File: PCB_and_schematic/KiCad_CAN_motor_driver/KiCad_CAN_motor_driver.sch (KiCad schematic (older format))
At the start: 59 parts, among them J1 SWDIO, J2 UART, J3 POWER IN 24V, J4 MOTOR OUT, J5 CAN, J6 PWM IN, Q1 BTN8982TA, Q2 BTN8982TA, U1 SN65HVD232, U2 LMR50410, U3 STM32F103C8Tx

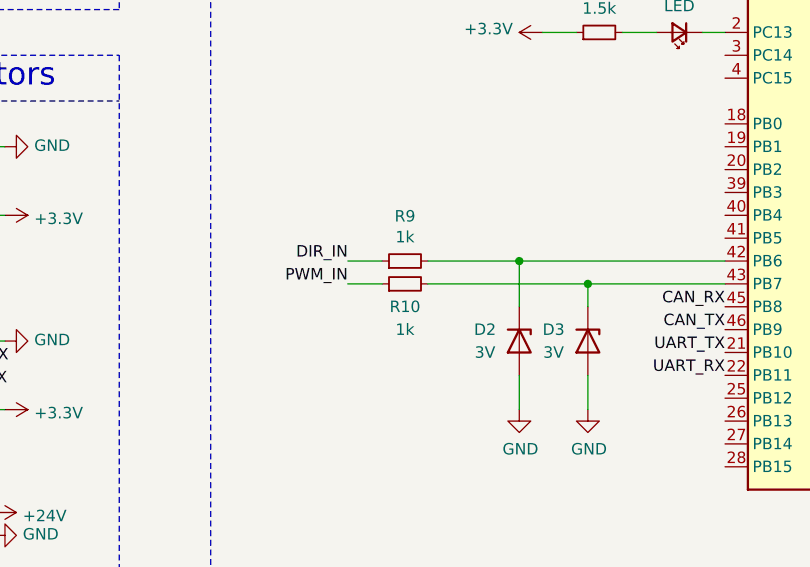
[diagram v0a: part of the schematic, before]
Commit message: PDF schematic
+ schematic in PDF format for quick preview
+ changed resistors on PWM inputs from 1K to 6.8K to decrease Zener diodes current
+ little tweaks in PCB traces
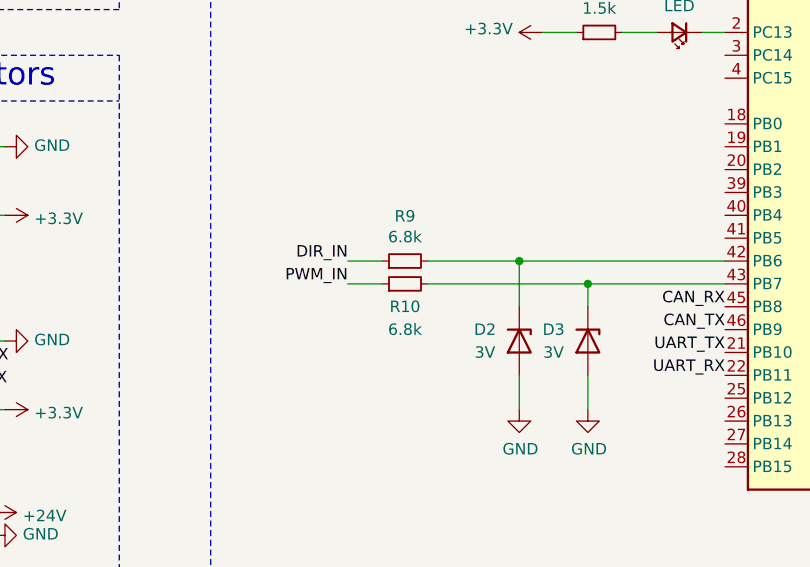
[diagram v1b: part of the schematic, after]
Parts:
- R10, R9: value 1k -> 6.8k
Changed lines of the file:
@@
 P 8650 4850
 F 0 "R9" V 8846 4850 50  0000 C CNN
-F 1 "1k" V 8755 4850 50  0000 C CNN
+F 1 "6.8k" V 8755 4850 50  0000 C CNN
 F 2 "Resistor_SMD:R_1206_3216Metric_Pad1.30x1.75mm_HandSolder" H 8650 4850 50  0001 C CNN
 F 3 "~" H 8650 4850 50  0001 C CNN
@@
 P 8650 4950
 F 0 "R10" V 8550 4950 50  0000 C CNN
-F 1 "1k" V 8450 4950 50  0000 C CNN
+F 1 "6.8k" V 8450 4950 50  0000 C CNN
 F 2 "Resistor_SMD:R_1206_3216Metric_Pad1.30x1.75mm_HandSolder" H 8650 4950 50  0001 C CNN
 F 3 "~" H 8650 4950 50  0001 C CNN

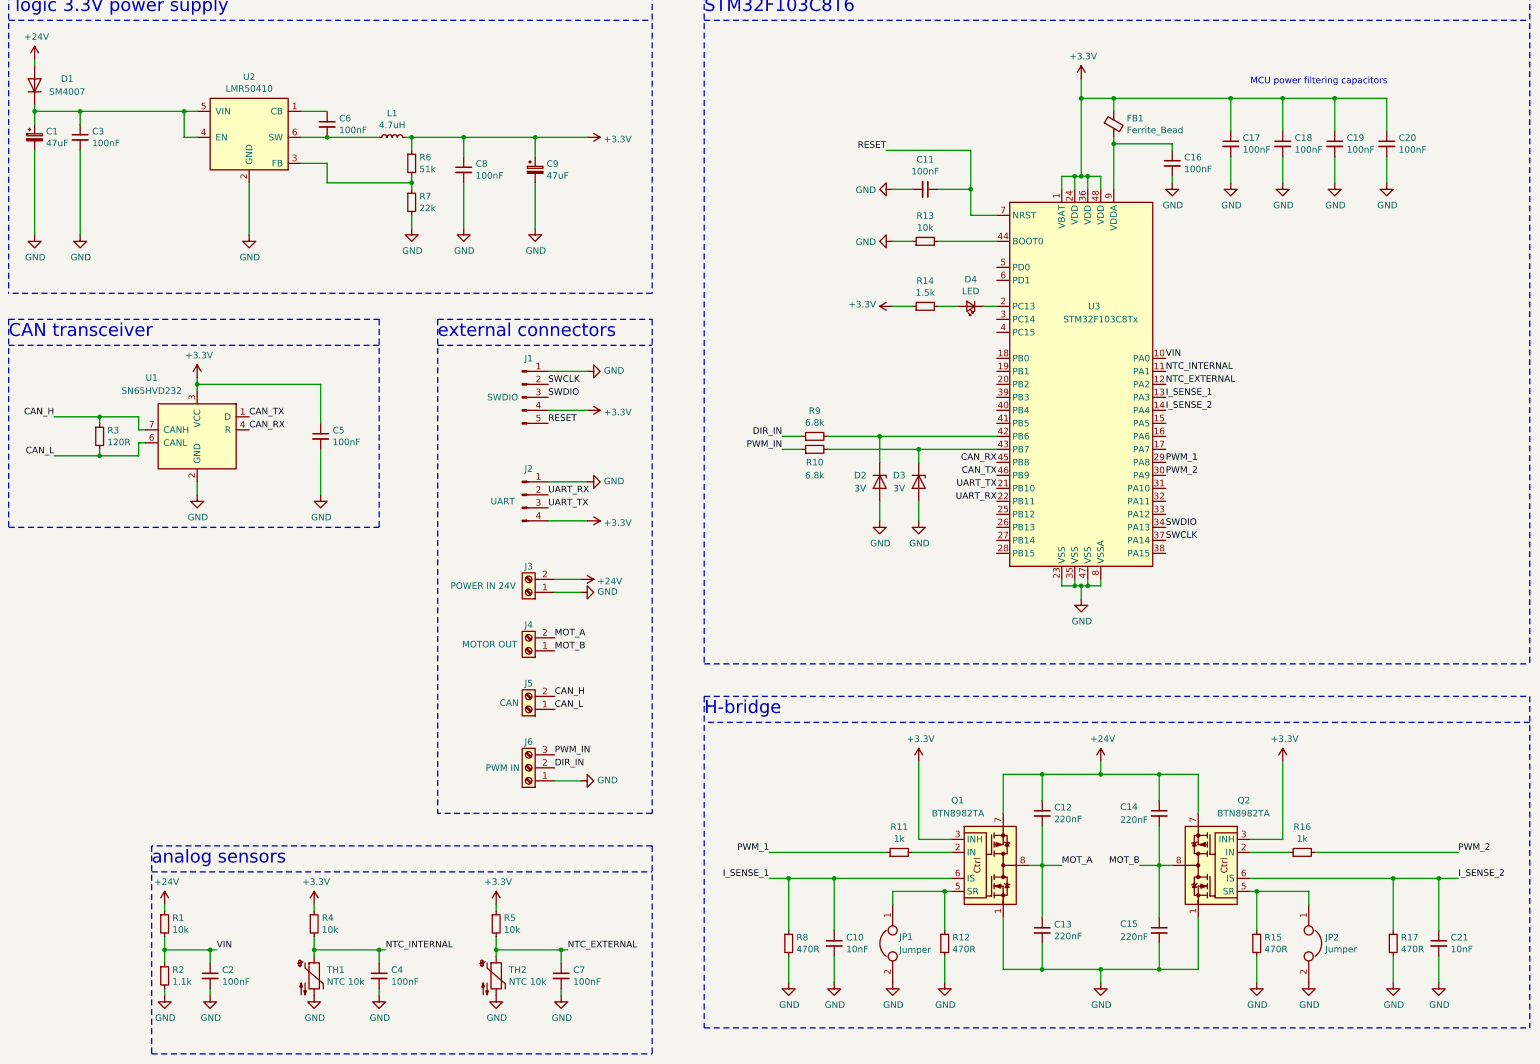
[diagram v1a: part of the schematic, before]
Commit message: Added vias on power traces near input, added testpoints
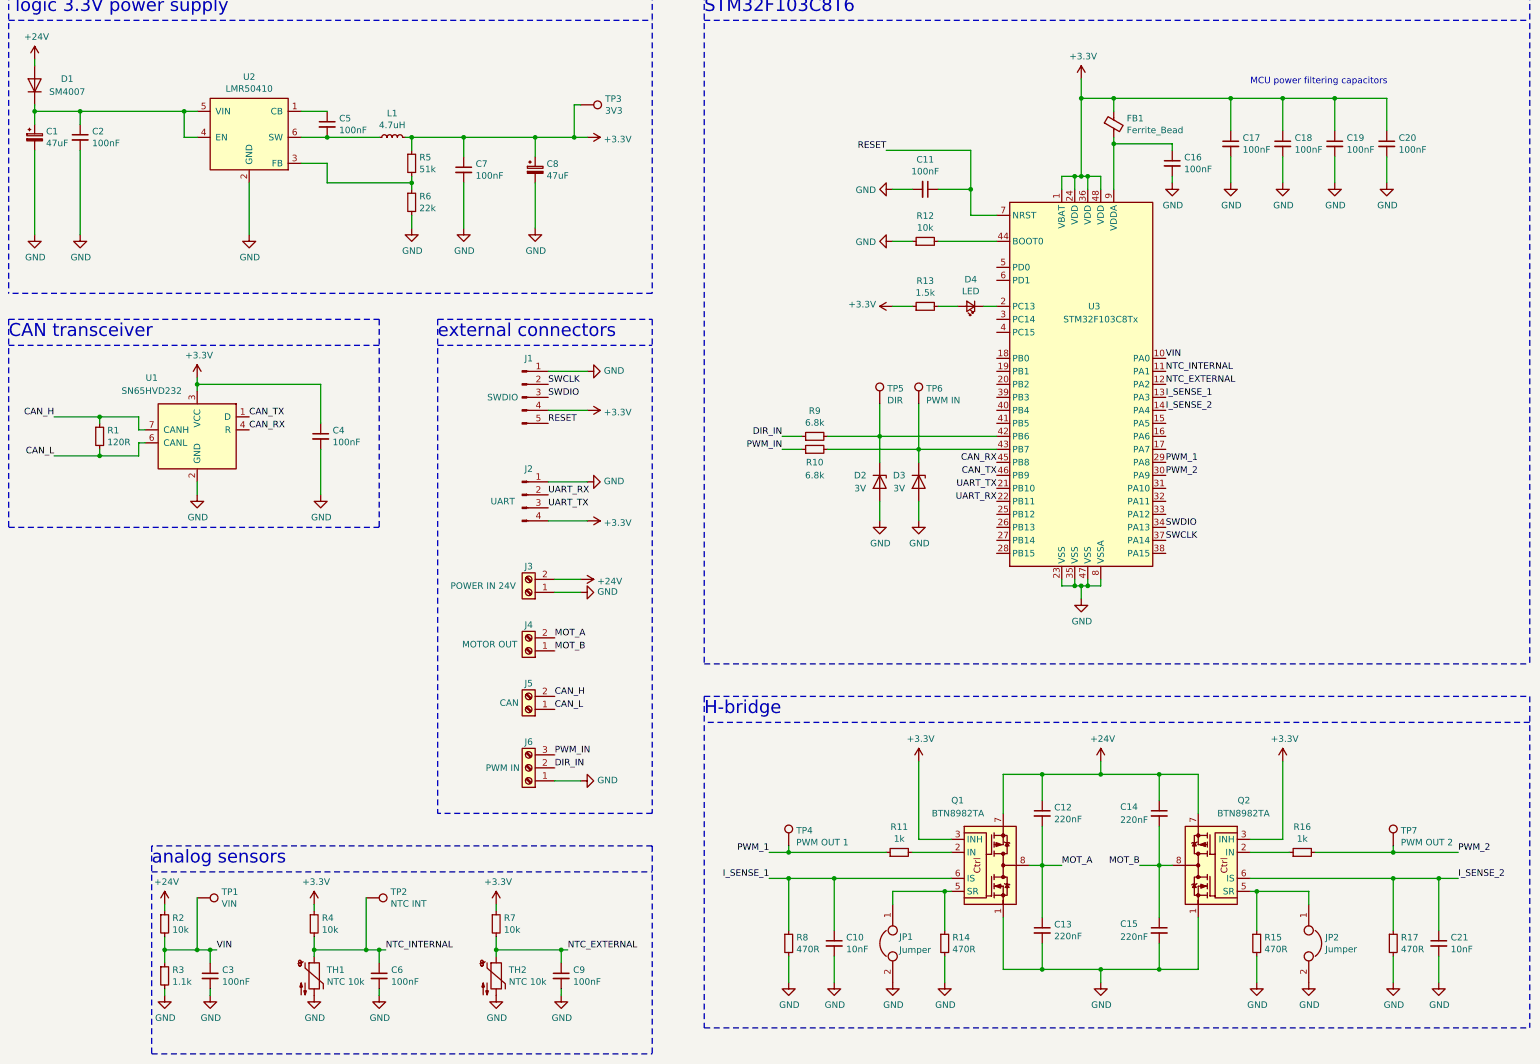
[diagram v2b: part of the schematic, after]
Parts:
- added TP1: VIN, TestPoint:TestPoint_THTPad_D1.0mm_Drill0.5mm, symbol Connector:TestPoint
- added TP2: NTC INT, TestPoint:TestPoint_THTPad_D1.0mm_Drill0.5mm, symbol Connector:TestPoint
- added TP3: 3V3, TestPoint:TestPoint_THTPad_D1.0mm_Drill0.5mm, symbol Connector:TestPoint
- added TP4: PWM OUT 1, TestPoint:TestPoint_THTPad_D1.0mm_Drill0.5mm, symbol Connector:TestPoint
- added TP5: DIR, TestPoint:TestPoint_THTPad_D1.0mm_Drill0.5mm, symbol Connector:TestPoint
- added TP6: PWM IN, TestPoint:TestPoint_THTPad_D1.0mm_Drill0.5mm, symbol Connector:TestPoint
- added TP7: PWM OUT 2, TestPoint:TestPoint_THTPad_D1.0mm_Drill0.5mm, symbol Connector:TestPoint
- renumbered C3 to C2, C2 to C3, C5 to C4, C6 to C5, C4 to C6, C8 to C7, C9 to C8, C7 to C9, R3 to R1, R13 to R12, R14 to R13, R12 to R14, R1 to R2, R2 to R3, R6 to R5, R7 to R6, R5 to R7
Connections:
- net +3V3: now also TP3.1
- net NTC_INTERNAL: now also TP2.1
- net PWM_1: now also TP4.1
- net PWM_2: now also TP7.1
- net VIN: now also TP1.1
- net at D2.1 (K), R9.2, U3.42 (PB6): now also TP5.1
- net at D3.1 (K), R10.2, U3.43 (PB7): now also TP6.1

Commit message: Final PCB version (rev 1.0)
+ reduced amount of vias
+ increased distance between vias
+ removed vias from half-bridge's bottom and moved them closer to motor output pads
+ changed PWM input connector to goldpin
+ added jumper (default open) connecting terminating resistor to CAN bus

+ updated PDF schematic
+updated 3D models
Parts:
- removed J6: PWM IN, WK_lib:PowerPad_3x_3mm, symbol Connector:Screw_Terminal_01x03
- added J6: PWM_IN, Connector_PinHeader_2.54mm:PinHeader_1x03_P2.54mm_Vertical, symbol Connector:Conn_01x03_Male
- added JP3: Jumper, Jumper:SolderJumper-2_P1.3mm_Open_Pad1.0x1.5mm, symbol Device:Jumper
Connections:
- net CAN_L: now also JP3.2; no longer R1.2
- net DIR_IN: now also J6.2 (Pin_2)
- net GND: now also J6.3 (Pin_3)
- net PWM_IN: now also J6.1 (Pin_1)
- new net: JP3.1, R1.2
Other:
- moved on the sheet: R1
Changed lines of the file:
@@
 Text Label 6650 6850 0    50   ~ 0
 CAN_H
-$Comp
-L Connector:Screw_Terminal_01x03 J6
-U 1 1 6063F28F
-P 6450 7400
-F 0 "J6" H 6450 7200 50  0000 C CNN
-F 1 "PWM IN" H 6650 7400 50  0000 C CNN
-F 2 "WK_lib:PowerPad_3x_3mm" H 6450 7400 50  0001 C CNN
-F 3 "~" H 6450 7400 50  0001 C CNN
-	1    6450 7400
-	-1   0    0    1
-$EndComp
 Text Label 6650 7300 0    50   ~ 0
 PWM_IN
@@
 $EndComp
 Wire Wire Line
-	6650 7500 6850 7500
+	6600 7500 6850 7500
 Wire Notes Line
 	7400 7750 5750 7750
@@
 Wire Notes Line
 	5750 3950 5750 7750
-$Comp
-L Interface_CAN_LIN:SN65HVD232 U1
-U 1 1 60673CE3
-P 3900 4800
-F 0 "U1" H 4250 5200 50  0000 C CNN
-F 1 "SN65HVD232" H 4250 5100 50  0000 C CNN
-F 2 "Package_SO:SOIC-8_3.9x4.9mm_P1.27mm" H 3900 4300 50  0001 C CNN
-F 3 "http://www.ti.com/lit/ds/symlink/sn65hvd230.pdf" H 3800 5200 50  0001 C CNN
-	1    3900 4800
-	-1   0    0    -1
-$EndComp
-$Comp
-L power:+3.3V #PWR06
-U 1 1 60676560
-P 3900 4400
-F 0 "#PWR06" H 3900 4250 50  0001 C CNN
-F 1 "+3.3V" H 3915 4573 50  0000 C CNN
-F 2 "" H 3900 4400 50  0001 C CNN
-F 3 "" H 3900 4400 50  0001 C CNN
-	1    3900 4400
-	1    0    0    -1
-$EndComp
-$Comp
-L power:GND #PWR07
-U 1 1 606775A4
-P 3900 5300
-F 0 "#PWR07" H 3900 5050 50  0001 C CNN
-F 1 "GND" H 3905 5127 50  0000 C CNN
-F 2 "" H 3900 5300 50  0001 C CNN
-F 3 "" H 3900 5300 50  0001 C CNN
-	1    3900 5300
-	1    0    0    -1
-$EndComp
-Text Label 4300 4700 0    50   ~ 0
-CAN_TX
-Text Label 4300 4800 0    50   ~ 0
-CAN_RX
-Wire Wire Line
-	3900 4400 3900 4450
-Wire Wire Line
-	3900 5200 3900 5300
-Text Label 2800 4700 2    50   ~ 0
-CAN_H
-Text Label 2800 5000 2    50   ~ 0
-CAN_L
-$Comp
-L Device:R_Small R1
-U 1 1 60686C82
-P 3150 4850
-F 0 "R1" H 3209 4896 50  0000 L CNN
-F 1 "120R" H 3209 4805 50  0000 L CNN
-F 2 "Resistor_SMD:R_1206_3216Metric_Pad1.30x1.75mm_HandSolder" H 3150 4850 50  0001 C CNN
-F 3 "~" H 3150 4850 50  0001 C CNN
-	1    3150 4850
-	1    0    0    -1
-$EndComp
-Wire Wire Line
-	3500 4800 3450 4800
-Wire Wire Line
-	3450 4800 3450 4700
-Wire Wire Line
-	3450 4700 3150 4700
-Wire Wire Line
-	3500 4900 3450 4900
-Wire Wire Line
-	3450 4900 3450 5000
-Wire Wire Line
-	3450 5000 3150 5000
-Wire Wire Line
-	3150 4950 3150 5000
-Connection ~ 3150 5000
-Wire Wire Line
-	3150 5000 2800 5000
-Wire Wire Line
-	3150 4750 3150 4700
-Connection ~ 3150 4700
-Wire Wire Line
-	3150 4700 2800 4700
-$Comp
-L Device:C_Small C4
-U 1 1 606A1169
-P 4850 4850
-F 0 "C4" H 4942 4896 50  0000 L CNN
-F 1 "100nF" H 4942 4805 50  0000 L CNN
-F 2 "Capacitor_SMD:C_1206_3216Metric_Pad1.33x1.80mm_HandSolder" H 4850 4850 50  0001 C CNN
-F 3 "~" H 4850 4850 50  0001 C CNN
-	1    4850 4850
-	1    0    0    -1
-$EndComp
-Wire Wire Line
-	3900 4450 4850 4450
-Wire Wire Line
-	4850 4450 4850 4750
-Connection ~ 3900 4450
-Wire Wire Line
-	3900 4450 3900 4500
-Wire Wire Line
-	4850 4950 4850 5300
-$Comp
-L power:GND #PWR012
-U 1 1 606AA75D
-P 4850 5300
-F 0 "#PWR012" H 4850 5050 50  0001 C CNN
-F 1 "GND" H 4855 5127 50  0000 C CNN
-F 2 "" H 4850 5300 50  0001 C CNN
-F 3 "" H 4850 5300 50  0001 C CNN
-	1    4850 5300
-	1    0    0    -1
-$EndComp
 Wire Notes Line
 	5300 4150 2450 4150
@@
 Wire Wire Line
 	6200 8800 6700 8800
+$Comp
+L Connector:Conn_01x03_Male J6
+U 1 1 605AD111
+P 6400 7400
+F 0 "J6" H 6450 7600 50  0000 C CNN
+F 1 "PWM_IN" H 6250 7400 50  0000 C CNN
+F 2 "Connector_PinHeader_2.54mm:PinHeader_1x03_P2.54mm_Vertical" H 6400 7400 50  0001 C CNN
+F 3 "~" H 6400 7400 50  0001 C CNN
+	1    6400 7400
+	1    0    0    -1
+$EndComp
+Wire Wire Line
+	6650 7300 6600 7300
+Wire Wire Line
+	6650 7400 6600 7400
+$Comp
+L power:GND #PWR012
+U 1 1 606AA75D
+P 4850 5300
+F 0 "#PWR012" H 4850 5050 50  0001 C CNN
+F 1 "GND" H 4855 5127 50  0000 C CNN
+F 2 "" H 4850 5300 50  0001 C CNN
+F 3 "" H 4850 5300 50  0001 C CNN
+	1    4850 5300
+	1    0    0    -1
+$EndComp
+Wire Wire Line
+	4850 4950 4850 5300
+Wire Wire Line
+	3900 4450 3900 4500
+Connection ~ 3900 4450
+Wire Wire Line
+	4850 4450 4850 4750
+Wire Wire Line
+	3900 4450 4850 4450
+$Comp
+L Device:C_Small C4
+U 1 1 606A1169
+P 4850 4850
+F 0 "C4" H 4942 4896 50  0000 L CNN
+F 1 "100nF" H 4942 4805 50  0000 L CNN
+F 2 "Capacitor_SMD:C_1206_3216Metric_Pad1.33x1.80mm_HandSolder" H 4850 4850 50  0001 C CNN
+F 3 "~" H 4850 4850 50  0001 C CNN
+	1    4850 4850
+	1    0    0    -1
+$EndComp
+Wire Wire Line
+	3100 4400 2750 4400
+Connection ~ 3100 4400
+Wire Wire Line
+	3100 4450 3100 4400
+Wire Wire Line
+	3100 5350 2750 5350
+Connection ~ 3100 5350
+Wire Wire Line
+	3100 5300 3100 5350
+Wire Wire Line
+	3500 4900 3450 4900
+Wire Wire Line
+	3500 4800 3450 4800
+$Comp
+L Device:R_Small R1
+U 1 1 60686C82
+P 3100 4550
+F 0 "R1" H 3159 4596 50  0000 L CNN
+F 1 "120R" H 3159 4505 50  0000 L CNN
+F 2 "Resistor_SMD:R_1206_3216Metric_Pad1.30x1.75mm_HandSolder" H 3100 4550 50  0001 C CNN
+F 3 "~" H 3100 4550 50  0001 C CNN
+	1    3100 4550
+	1    0    0    -1
+$EndComp
+Wire Wire Line
+	3900 5200 3900 5300
+Wire Wire Line
+	3900 4400 3900 4450
+Text Label 4300 4800 0    50   ~ 0
+CAN_RX
+Text Label 4300 4700 0    50   ~ 0
+CAN_TX
+$Comp
+L power:GND #PWR07
+U 1 1 606775A4
+P 3900 5300
+F 0 "#PWR07" H 3900 5050 50  0001 C CNN
+F 1 "GND" H 3905 5127 50  0000 C CNN
+F 2 "" H 3900 5300 50  0001 C CNN
+F 3 "" H 3900 5300 50  0001 C CNN
+	1    3900 5300
+	1    0    0    -1
+$EndComp
+$Comp
+L power:+3.3V #PWR06
+U 1 1 60676560
+P 3900 4400
+F 0 "#PWR06" H 3900 4250 50  0001 C CNN
+F 1 "+3.3V" H 3915 4573 50  0000 C CNN
+F 2 "" H 3900 4400 50  0001 C CNN
+F 3 "" H 3900 4400 50  0001 C CNN
+	1    3900 4400
+	1    0    0    -1
+$EndComp
+$Comp
+L Interface_CAN_LIN:SN65HVD232 U1
+U 1 1 60673CE3
+P 3900 4800
+F 0 "U1" H 3450 4400 50  0000 C CNN
+F 1 "SN65HVD232" H 3450 4300 50  0000 C CNN
+F 2 "Package_SO:SOIC-8_3.9x4.9mm_P1.27mm" H 3900 4300 50  0001 C CNN
+F 3 "http://www.ti.com/lit/ds/symlink/sn65hvd230.pdf" H 3800 5200 50  0001 C CNN
+	1    3900 4800
+	-1   0    0    -1
+$EndComp
+Text Label 2750 5350 2    50   ~ 0
+CAN_L
+Text Label 2750 4400 2    50   ~ 0
+CAN_H
+$Comp
+L Device:Jumper JP3
+U 1 1 6072D659
+P 3100 5000
+F 0 "JP3" V 3050 4950 50  0000 R CNN
+F 1 "Jumper" V 3150 4950 50  0000 R CNN
+F 2 "Jumper:SolderJumper-2_P1.3mm_Open_Pad1.0x1.5mm" H 3100 5000 50  0001 C CNN
+F 3 "~" H 3100 5000 50  0001 C CNN
+	1    3100 5000
+	0    -1   1    0
+$EndComp
+Wire Wire Line
+	3100 4400 3450 4400
+Wire Wire Line
+	3450 4400 3450 4800
+Wire Wire Line
+	3100 5350 3450 5350
+Wire Wire Line
+	3450 4900 3450 5350
+Wire Wire Line
+	3100 4700 3100 4650
 $EndSCHEMATC
